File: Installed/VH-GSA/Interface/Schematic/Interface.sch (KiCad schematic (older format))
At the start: 29 parts, among them J1 RJ12, J2 RJ45, P1 USB_B, P10 USB_A, P11 USB_A, P12 USB_A, P13 USB_A, P14 USB_A, P15 USB_A, P16 USB_A, P17 USB_A, P2 USB_B, P3 CONN_01X02, P4 USB_B, P5 USB_B, P6 CONN_01X06, P7 CONN_01X06, P8 CONN_01X06, P9 CONN_01X06, U1 MAX232

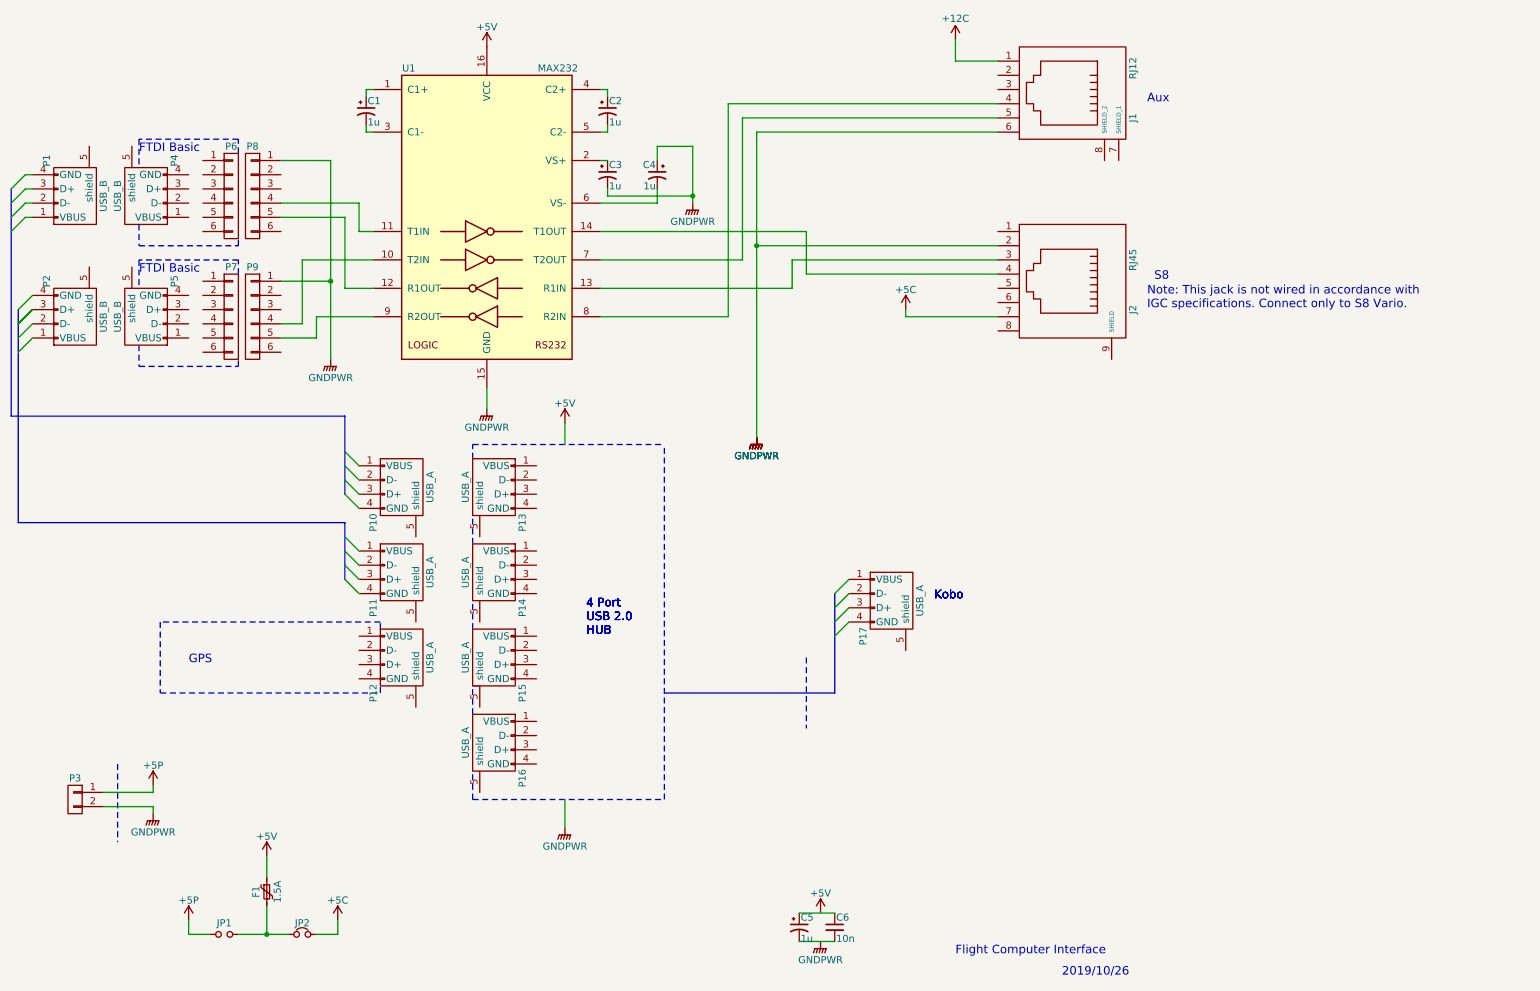
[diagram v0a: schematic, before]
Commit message: VH-GSA: Re annotated schematics
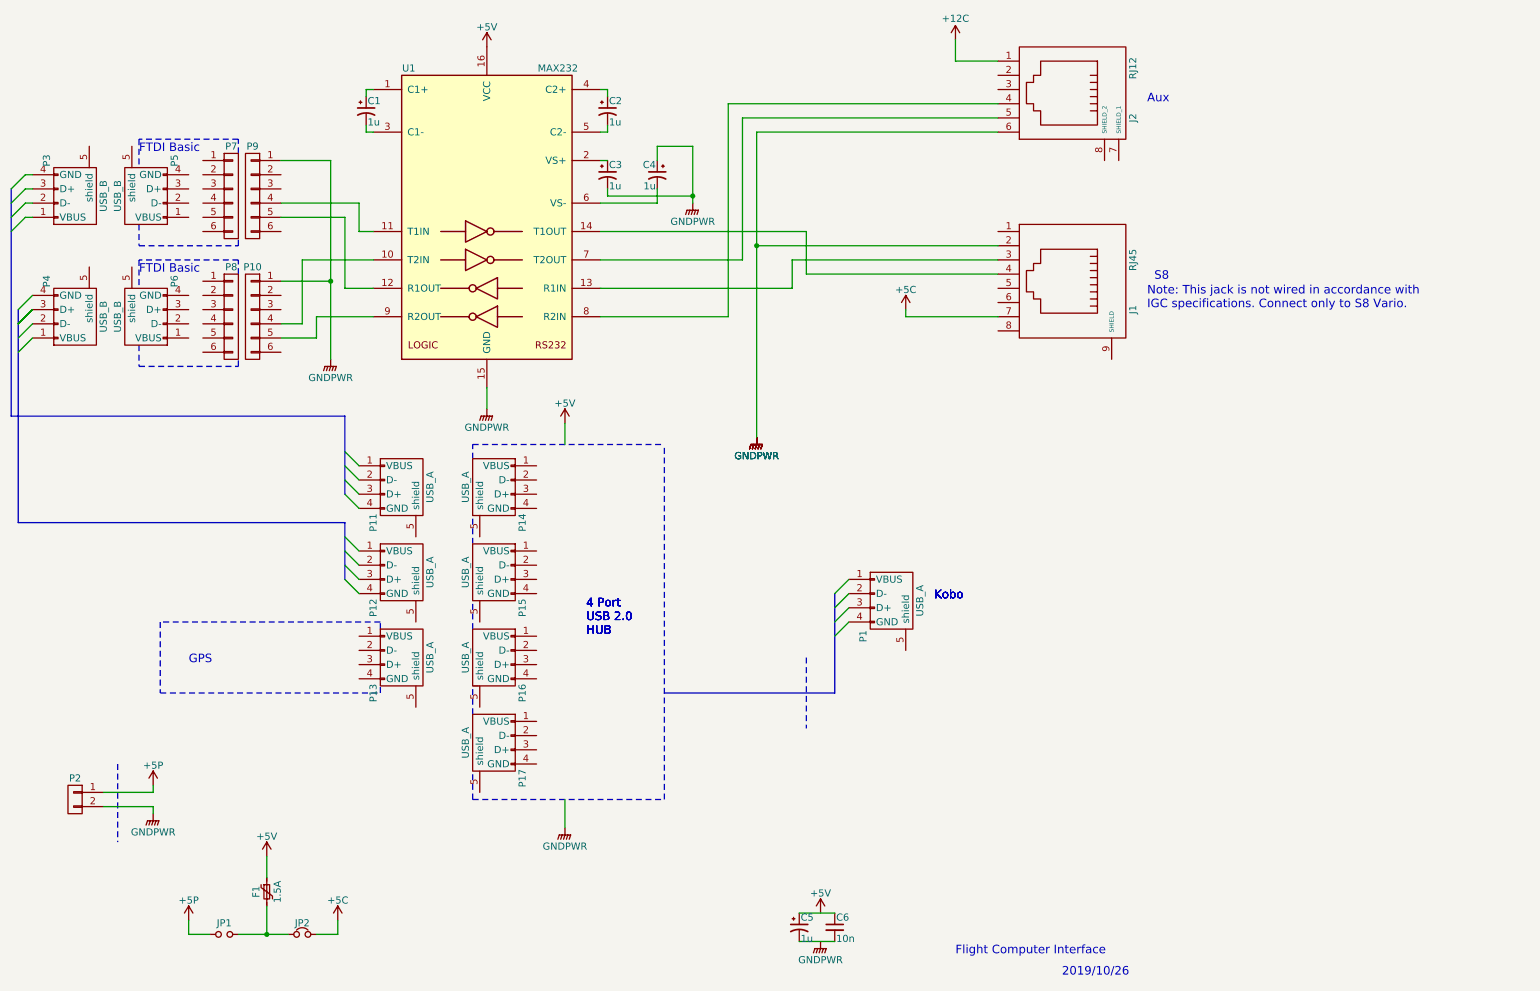
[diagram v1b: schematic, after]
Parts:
- renumbered J2 to J1, J1 to J2, P17 to P1, P9 to P10, P10 to P11, P11 to P12, P12 to P13, P13 to P14, P14 to P15, P15 to P16, P16 to P17, P3 to P2, P1 to P3, P2 to P4, P4 to P5, P5 to P6, P6 to P7, P7 to P8, P8 to P9
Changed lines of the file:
@@
 $EndComp
 $Comp
-L RJ12 J1
+L RJ12 J2
 U 1 1 5D9B4F4C
 P 8150 1400
-F 0 "J1" H 8350 1900 50  0000 C CNN
+F 0 "J2" H 8350 1900 50  0000 C CNN
 F 1 "RJ12" H 8000 1900 50  0000 C CNN
 F 2 "" H 8150 1400 50  0000 C CNN
@@
 $EndComp
 $Comp
-L CONN_01X06 P6
+L CONN_01X06 P7
 U 1 1 5D9BB2B6
 P 2300 2150
-F 0 "P6" H 2300 2500 50  0000 C CNN
+F 0 "P7" H 2300 2500 50  0000 C CNN
 F 1 "CONN_01X06" V 2400 2150 50  0001 C CNN
 F 2 "" H 2300 2150 50  0000 C CNN
@@
 $EndComp
 $Comp
-L CONN_01X06 P8
+L CONN_01X06 P9
 U 1 1 5D9BB331
 P 2450 2150
-F 0 "P8" H 2450 2500 50  0000 C CNN
+F 0 "P9" H 2450 2500 50  0000 C CNN
 F 1 "CONN_01X06" V 2550 2150 50  0001 C CNN
 F 2 "" H 2450 2150 50  0000 C CNN
@@
 $EndComp
 $Comp
-L CONN_01X06 P9
+L CONN_01X06 P10
 U 1 1 5D9BB3AC
 P 2450 3000
-F 0 "P9" H 2450 3350 50  0000 C CNN
+F 0 "P10" H 2450 3350 50  0000 C CNN
 F 1 "CONN_01X06" V 2550 3000 50  0001 C CNN
 F 2 "" H 2450 3000 50  0000 C CNN
@@
 $EndComp
 $Comp
-L CONN_01X06 P7
+L CONN_01X06 P8
 U 1 1 5D9BB3FD
 P 2300 3000
-F 0 "P7" H 2300 3350 50  0000 C CNN
+F 0 "P8" H 2300 3350 50  0000 C CNN
 F 1 "CONN_01X06" V 2400 3000 50  0001 C CNN
 F 2 "" H 2300 3000 50  0000 C CNN
@@
 $EndComp
 $Comp
-L GNDPWR #PWR11
+L GNDPWR #PWR211
 U 1 1 5D9D903E
 P 5550 2200
-F 0 "#PWR11" H 5550 2000 50  0001 C CNN
+F 0 "#PWR211" H 5550 2000 50  0001 C CNN
 F 1 "GNDPWR" H 5550 2070 50  0000 C CNN
 F 2 "" H 5550 2150 50  0000 C CNN
@@
 $EndComp
 $Comp
-L USB_B P4
+L USB_B P5
 U 1 1 5D9D9EF6
 P 1700 2100
-F 0 "P4" H 1900 1900 50  0000 C CNN
+F 0 "P5" H 1900 1900 50  0000 C CNN
 F 1 "USB_B" H 1650 2300 50  0000 C CNN
 F 2 "" V 1650 2000 50  0000 C CNN
@@
 $EndComp
 $Comp
-L USB_B P5
+L USB_B P6
 U 1 1 5D9DA106
 P 1700 2950
-F 0 "P5" H 1900 2750 50  0000 C CNN
+F 0 "P6" H 1900 2750 50  0000 C CNN
 F 1 "USB_B" H 1650 3150 50  0000 C CNN
 F 2 "" V 1650 2850 50  0000 C CNN
@@
 $EndComp
 $Comp
-L GNDPWR #PWR8
+L GNDPWR #PWR208
 U 1 1 5D9E150F
 P 4100 3650
-F 0 "#PWR8" H 4100 3450 50  0001 C CNN
+F 0 "#PWR208" H 4100 3450 50  0001 C CNN
 F 1 "GNDPWR" H 4100 3520 50  0000 C CNN
 F 2 "" H 4100 3600 50  0000 C CNN
@@
 $EndComp
 $Comp
-L GNDPWR #PWR17
+L GNDPWR #PWR217
 U 1 1 5D9E30CE
 P 6450 7400
-F 0 "#PWR17" H 6450 7200 50  0001 C CNN
+F 0 "#PWR217" H 6450 7200 50  0001 C CNN
 F 1 "GNDPWR" H 6450 7270 50  0000 C CNN
 F 2 "" H 6450 7350 50  0000 C CNN
@@
 $EndComp
 $Comp
-L +5V #PWR16
+L +5V #PWR216
 U 1 1 5D9E314B
 P 6450 7200
-F 0 "#PWR16" H 6450 7050 50  0001 C CNN
+F 0 "#PWR216" H 6450 7050 50  0001 C CNN
 F 1 "+5V" H 6450 7340 50  0000 C CNN
 F 2 "" H 6450 7200 50  0000 C CNN
@@
 $EndComp
 $Comp
-L USB_A P15
+L USB_A P16
 U 1 1 5D9E4C0E
 P 4150 5450
-F 0 "P15" H 4350 5250 50  0000 C CNN
+F 0 "P16" H 4350 5250 50  0000 C CNN
 F 1 "USB_A" H 4100 5650 50  0000 C CNN
 F 2 "" V 4100 5350 50  0000 C CNN
@@
 $EndComp
 $Comp
-L USB_A P16
+L USB_A P17
 U 1 1 5D9E4C7F
 P 4150 6050
-F 0 "P16" H 4350 5850 50  0000 C CNN
+F 0 "P17" H 4350 5850 50  0000 C CNN
 F 1 "USB_A" H 4100 6250 50  0000 C CNN
 F 2 "" V 4100 5950 50  0000 C CNN
@@
 $EndComp
 $Comp
-L USB_A P14
+L USB_A P15
 U 1 1 5D9E4D7F
 P 4150 4850
-F 0 "P14" H 4350 4650 50  0000 C CNN
+F 0 "P15" H 4350 4650 50  0000 C CNN
 F 1 "USB_A" H 4100 5050 50  0000 C CNN
 F 2 "" V 4100 4750 50  0000 C CNN
@@
 $EndComp
 $Comp
-L USB_A P13
+L USB_A P14
 U 1 1 5D9E4E2B
 P 4150 4250
-F 0 "P13" H 4350 4050 50  0000 C CNN
+F 0 "P14" H 4350 4050 50  0000 C CNN
 F 1 "USB_A" H 4100 4450 50  0000 C CNN
 F 2 "" V 4100 4150 50  0000 C CNN
@@
 $EndComp
 $Comp
-L USB_A P17
+L USB_A P1
 U 1 1 5D9E4F55
 P 6950 5050
-F 0 "P17" H 7150 4850 50  0000 C CNN
+F 0 "P1" H 7150 4850 50  0000 C CNN
 F 1 "USB_A" H 6900 5250 50  0000 C CNN
 F 2 "" V 6900 4950 50  0000 C CNN
@@
 $EndComp
 $Comp
-L +5V #PWR7
+L +5V #PWR207
 U 1 1 5D9E5A35
 P 4100 1100
-F 0 "#PWR7" H 4100 950 50  0001 C CNN
+F 0 "#PWR207" H 4100 950 50  0001 C CNN
 F 1 "+5V" H 4100 1240 50  0000 C CNN
 F 2 "" H 4100 1100 50  0000 C CNN
@@
 $EndComp
 $Comp
-L USB_A P10
+L USB_A P11
 U 1 1 5D9E6B59
 P 3500 4250
-F 0 "P10" H 3700 4050 50  0000 C CNN
+F 0 "P11" H 3700 4050 50  0000 C CNN
 F 1 "USB_A" H 3450 4450 50  0000 C CNN
 F 2 "" V 3450 4150 50  0000 C CNN
@@
 $EndComp
 $Comp
-L USB_A P11
+L USB_A P12
 U 1 1 5D9E6BE9
 P 3500 4850
-F 0 "P11" H 3700 4650 50  0000 C CNN
+F 0 "P12" H 3700 4650 50  0000 C CNN
 F 1 "USB_A" H 3450 5050 50  0000 C CNN
 F 2 "" V 3450 4750 50  0000 C CNN
@@
 $EndComp
 $Comp
-L USB_B P1
+L USB_B P3
 U 1 1 5D9E7855
 P 1200 2100
-F 0 "P1" H 1400 1900 50  0000 C CNN
+F 0 "P3" H 1400 1900 50  0000 C CNN
 F 1 "USB_B" H 1150 2300 50  0000 C CNN
 F 2 "" V 1150 2000 50  0000 C CNN
@@
 	750  2400 850  2300
 $Comp
-L USB_B P2
+L USB_B P4
 U 1 1 5D9E7FA6
 P 1200 2950
-F 0 "P2" H 1400 2750 50  0000 C CNN
+F 0 "P4" H 1400 2750 50  0000 C CNN
 F 1 "USB_B" H 1150 3150 50  0000 C CNN
 F 2 "" V 1150 2850 50  0000 C CNN
@@
 	6550 5250 6650 5150
 $Comp
-L GNDPWR #PWR12
+L GNDPWR #PWR212
 U 1 1 5D9EC6E0
 P 6000 3850
-F 0 "#PWR12" H 6000 3650 50  0001 C CNN
+F 0 "#PWR212" H 6000 3650 50  0001 C CNN
 F 1 "GNDPWR" H 6000 3720 50  0000 C CNN
 F 2 "" H 6000 3800 50  0000 C CNN
@@
 Kobo
 $Comp
-L RJ45 J2
+L RJ45 J1
 U 1 1 5DA4AAC7
 P 8150 2750
-F 0 "J2" H 8350 3250 50  0000 C CNN
+F 0 "J1" H 8350 3250 50  0000 C CNN
 F 1 "RJ45" H 8000 3250 50  0000 C CNN
 F 2 "" H 8150 2750 50  0000 C CNN
@@
 $EndComp
 $Comp
-L +5V #PWR9
+L +5V #PWR209
 U 1 1 5DA4B908
 P 4650 3750
-F 0 "#PWR9" H 4650 3600 50  0001 C CNN
+F 0 "#PWR209" H 4650 3600 50  0001 C CNN
 F 1 "+5V" H 4650 3890 50  0000 C CNN
 F 2 "" H 4650 3750 50  0000 C CNN
@@
 $EndComp
 $Comp
-L GNDPWR #PWR10
+L GNDPWR #PWR210
 U 1 1 5DA4B9EC
 P 4650 6600
-F 0 "#PWR10" H 4650 6400 50  0001 C CNN
+F 0 "#PWR210" H 4650 6400 50  0001 C CNN
 F 1 "GNDPWR" H 4650 6470 50  0000 C CNN
 F 2 "" H 4650 6550 50  0000 C CNN
@@
 4 Port\nUSB 2.0\nHUB
 $Comp
-L GNDPWR #PWR13
+L GNDPWR #PWR213
 U 1 1 5DA4C0C2
 P 6000 3850
-F 0 "#PWR13" H 6000 3650 50  0001 C CNN
+F 0 "#PWR213" H 6000 3650 50  0001 C CNN
 F 1 "GNDPWR" H 6000 3720 50  0000 C CNN
 F 2 "" H 6000 3800 50  0000 C CNN
@@
 4 Port\nUSB 2.0\nHUB
 $Comp
-L GNDPWR #PWR14
+L GNDPWR #PWR214
 U 1 1 5DA4E40C
 P 6000 3850
-F 0 "#PWR14" H 6000 3650 50  0001 C CNN
+F 0 "#PWR214" H 6000 3650 50  0001 C CNN
 F 1 "GNDPWR" H 6000 3720 50  0000 C CNN
 F 2 "" H 6000 3800 50  0000 C CNN
@@
 4 Port\nUSB 2.0\nHUB
 $Comp
-L GNDPWR #PWR15
+L GNDPWR #PWR215
 U 1 1 5DA4E436
 P 6000 3850
-F 0 "#PWR15" H 6000 3650 50  0001 C CNN
+F 0 "#PWR215" H 6000 3650 50  0001 C CNN
 F 1 "GNDPWR" H 6000 3720 50  0000 C CNN
 F 2 "" H 6000 3800 50  0000 C CNN
@@
 Kobo
 $Comp
-L +5C #PWR18
+L +5C #PWR218
 U 1 1 5DA74C09
 P 7050 2950
-F 0 "#PWR18" H 7050 2800 50  0001 C CNN
+F 0 "#PWR218" H 7050 2800 50  0001 C CNN
 F 1 "+5C" H 7050 3090 50  0000 C CNN
 F 2 "" H 7050 2950 50  0000 C CNN
@@
 $EndComp
 $Comp
-L +5V #PWR4
+L +5V #PWR204
 U 1 1 5DA7581A
 P 2550 6800
-F 0 "#PWR4" H 2550 6650 50  0001 C CNN
+F 0 "#PWR204" H 2550 6650 50  0001 C CNN
 F 1 "+5V" H 2550 6940 50  0000 C CNN
 F 2 "" H 2550 6800 50  0000 C CNN
@@
 $EndComp
 $Comp
-L +5P #PWR3
+L +5P #PWR203
 U 1 1 5DA75885
 P 2000 7250
-F 0 "#PWR3" H 2000 7100 50  0001 C CNN
+F 0 "#PWR203" H 2000 7100 50  0001 C CNN
 F 1 "+5P" H 2000 7390 50  0000 C CNN
 F 2 "" H 2000 7250 50  0000 C CNN
@@
 $EndComp
 $Comp
-L +5C #PWR6
+L +5C #PWR206
 U 1 1 5DA758F0
 P 3050 7250
-F 0 "#PWR6" H 3050 7100 50  0001 C CNN
+F 0 "#PWR206" H 3050 7100 50  0001 C CNN
 F 1 "+5C" H 3050 7390 50  0000 C CNN
 F 2 "" H 3050 7250 50  0000 C CNN
@@
 $EndComp
 $Comp
-L USB_A P12
+L USB_A P13
 U 1 1 5DA766D1
 P 3500 5450
-F 0 "P12" H 3700 5250 50  0000 C CNN
+F 0 "P13" H 3700 5250 50  0000 C CNN
 F 1 "USB_A" H 3450 5650 50  0000 C CNN
 F 2 "" V 3450 5350 50  0000 C CNN
@@
 GPS
 $Comp
-L CONN_01X02 P3
+L CONN_01X02 P2
 U 1 1 5DA78DD3
 P 1200 6400
-F 0 "P3" H 1200 6550 50  0000 C CNN
+F 0 "P2" H 1200 6550 50  0000 C CNN
 F 1 "CONN_01X02" V 1300 6400 50  0001 C CNN
 F 2 "" H 1200 6400 50  0000 C CNN
@@
 $EndComp
 $Comp
-L +5P #PWR1
+L +5P #PWR201
 U 1 1 5DA7934A
 P 1750 6300
-F 0 "#PWR1" H 1750 6150 50  0001 C CNN
+F 0 "#PWR201" H 1750 6150 50  0001 C CNN
 F 1 "+5P" H 1750 6440 50  0000 C CNN
 F 2 "" H 1750 6300 50  0000 C CNN
@@
 $EndComp
 $Comp
-L GNDPWR #PWR2
+L GNDPWR #PWR202
 U 1 1 5DA79475
 P 1750 6500
-F 0 "#PWR2" H 1750 6300 50  0001 C CNN
+F 0 "#PWR202" H 1750 6300 50  0001 C CNN
 F 1 "GNDPWR" H 1750 6370 50  0000 C CNN
 F 2 "" H 1750 6450 50  0000 C CNN
@@
 $EndComp
 $Comp
-L GNDPWR #PWR5
+L GNDPWR #PWR205
 U 1 1 5DB1839A
 P 3000 3300
-F 0 "#PWR5" H 3000 3100 50  0001 C CNN
+F 0 "#PWR205" H 3000 3100 50  0001 C CNN
 F 1 "GNDPWR" H 3000 3170 50  0000 C CNN
 F 2 "" H 3000 3250 50  0000 C CNN
@@
 	5900 2600 5900 1600
 $Comp
-L +12C #PWR19
+L +12C #PWR219
 U 1 1 5DB44227
 P 7400 1050
-F 0 "#PWR19" H 7400 900 50  0001 C CNN
+F 0 "#PWR219" H 7400 900 50  0001 C CNN
 F 1 "+12C" H 7400 1200 50  0000 C CNN
 F 2 "" H 7400 1050 50  0000 C CNN

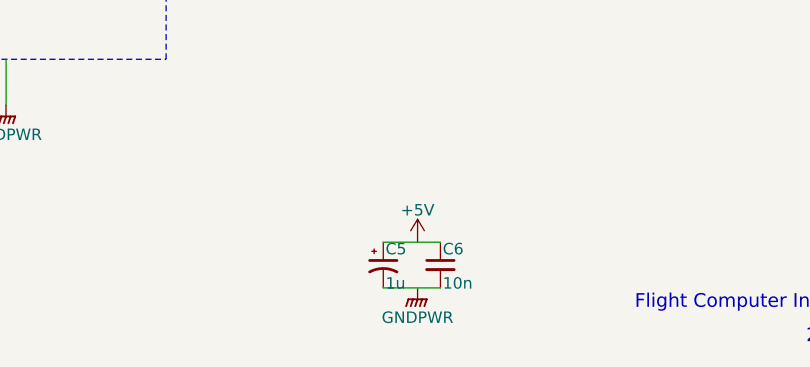
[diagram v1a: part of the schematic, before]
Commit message: VH-GSA: Changed 5V filter capacitor
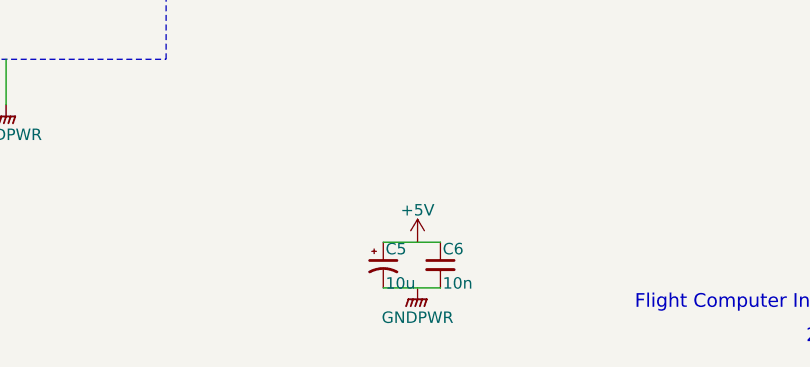
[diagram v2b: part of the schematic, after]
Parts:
- C5: value 1u -> 10u
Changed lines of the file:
@@
 P 6300 7300
 F 0 "C5" H 6310 7370 50  0000 L CNN
-F 1 "1u" H 6310 7220 50  0000 L CNN
+F 1 "10u" H 6310 7220 50  0000 L CNN
 F 2 "" H 6300 7300 50  0000 C CNN
 F 3 "" H 6300 7300 50  0000 C CNN
